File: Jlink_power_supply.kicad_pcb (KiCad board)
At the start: 2 copper layers, 36.2 x 33 mm, 4 parts, among them J1 Jlink input, J2 Supply select, J3 Jlink output, U1 AMS1117-3.3

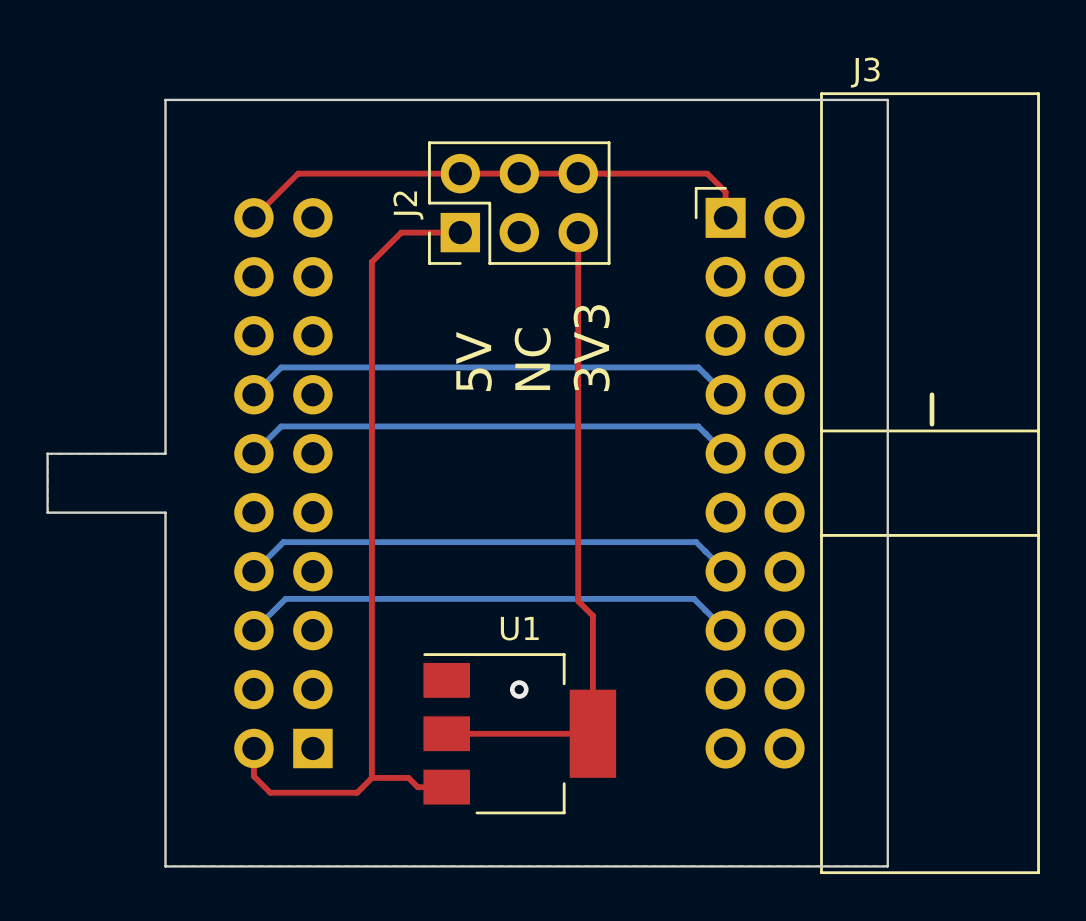
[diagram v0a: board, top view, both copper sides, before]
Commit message: Added capasitors for LDO and status led for 5V signal
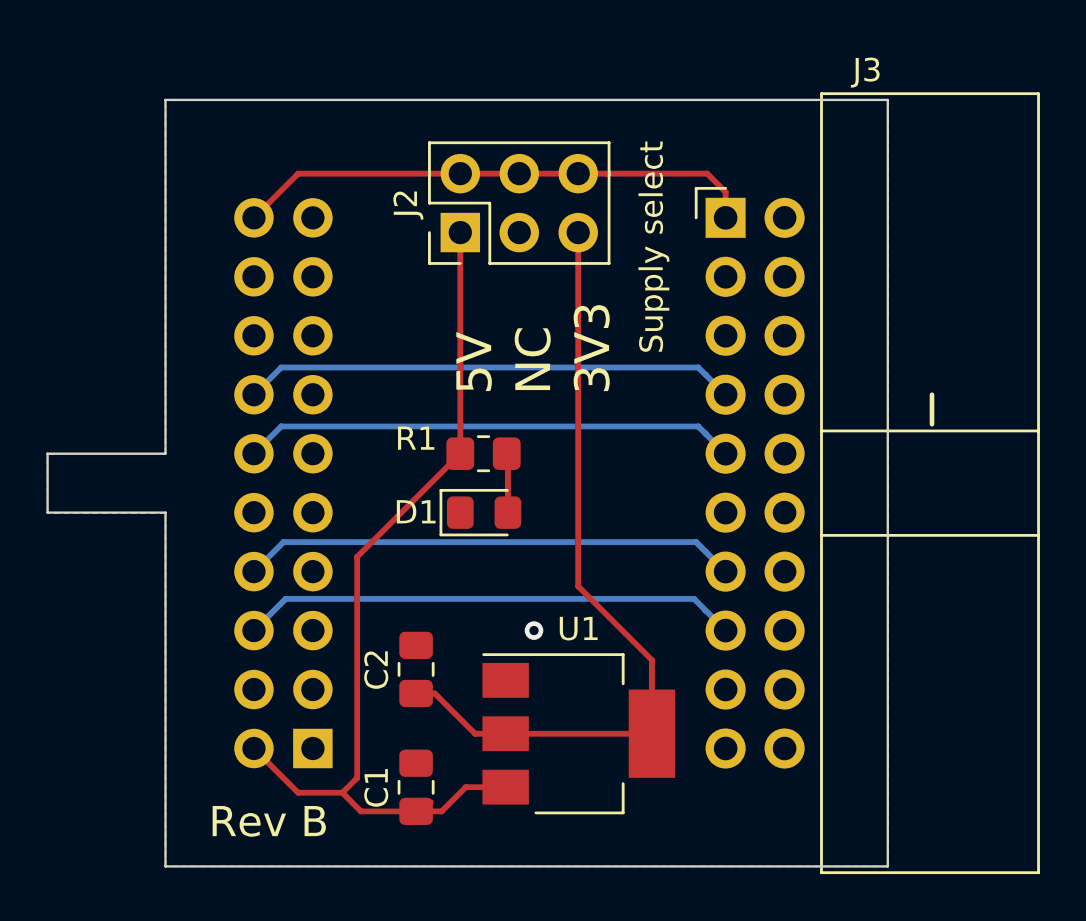
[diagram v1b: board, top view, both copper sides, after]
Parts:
- added C1: 10uF, Capacitor_SMD:C_0805_2012Metric_Pad1.18x1.45mm_HandSolder, F.Cu at (123.8, 121.1)
- added C2: 10uF, Capacitor_SMD:C_0805_2012Metric_Pad1.18x1.45mm_HandSolder, F.Cu at (123.8, 116.0)
- added D1: , LED_SMD:LED_0805_2012Metric_Pad1.15x1.40mm_HandSolder, F.Cu at (126.8, 109.2)
- added R1: , Resistor_SMD:R_0805_2012Metric_Pad1.20x1.40mm_HandSolder, F.Cu at (126.7, 106.7)
- moved U1 2.54 mm to (130.8, 118.7)
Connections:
- J1 pad 10: Net-(J1-Pad10) -> unconnected-(J1-Pad10)
- J1 pad 16: Net-(J1-Pad16) -> unconnected-(J1-Pad16)
- J1 pad 18: Net-(J1-Pad18) -> unconnected-(J1-Pad18)
- J1 pad 19: Net-(J1-Pad19) -> unconnected-(J1-Pad19)
- J1 pad 4: Net-(J1-Pad4) -> unconnected-(J1-Pad4)
- J2 pad 3: Net-(J2-Pad3) -> unconnected-(J2-Pad3)
- J3 pad 11: Net-(J3-Pad11) -> unconnected-(J3-Pad11)
- J3 pad 17: Net-(J3-Pad17) -> unconnected-(J3-Pad17)
- J3 pad 19: Net-(J3-Pad19) -> unconnected-(J3-Pad19)
- J3 pad 2: Net-(J3-Pad2) -> unconnected-(J3-Pad2)
- J3 pad 3: Net-(J3-Pad3) -> unconnected-(J3-Pad3)
- J3 pad 5: Net-(J3-Pad5) -> unconnected-(J3-Pad5)
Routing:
- net +3V3: track 28.2 -> 33.8 mm
- net Net-(R1-Pad1): track 0.00 -> 2.60 mm
- net +5V: track 36.8 -> 38.9 mm
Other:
- net class Default removed
- board text added: "Rev B"
